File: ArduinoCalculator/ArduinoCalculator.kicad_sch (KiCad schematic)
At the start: 1 part, among them U1 NORA-W106-00B

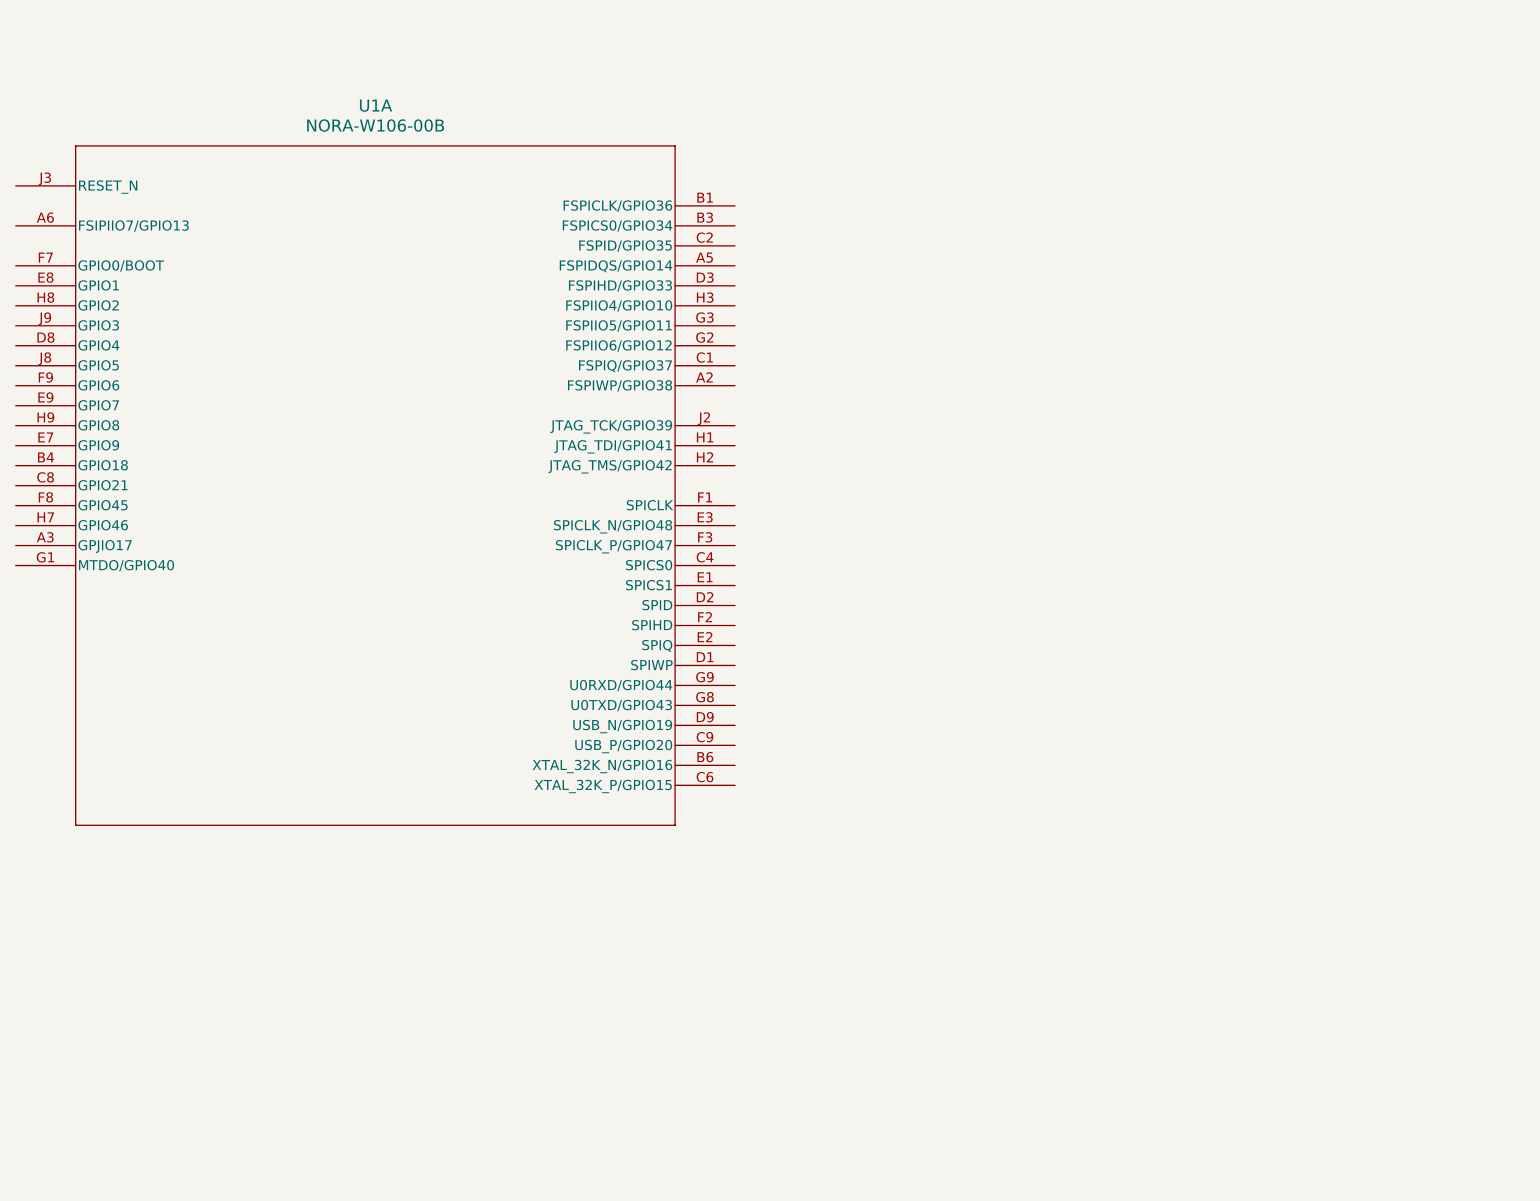
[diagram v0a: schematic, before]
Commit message: added NORA model
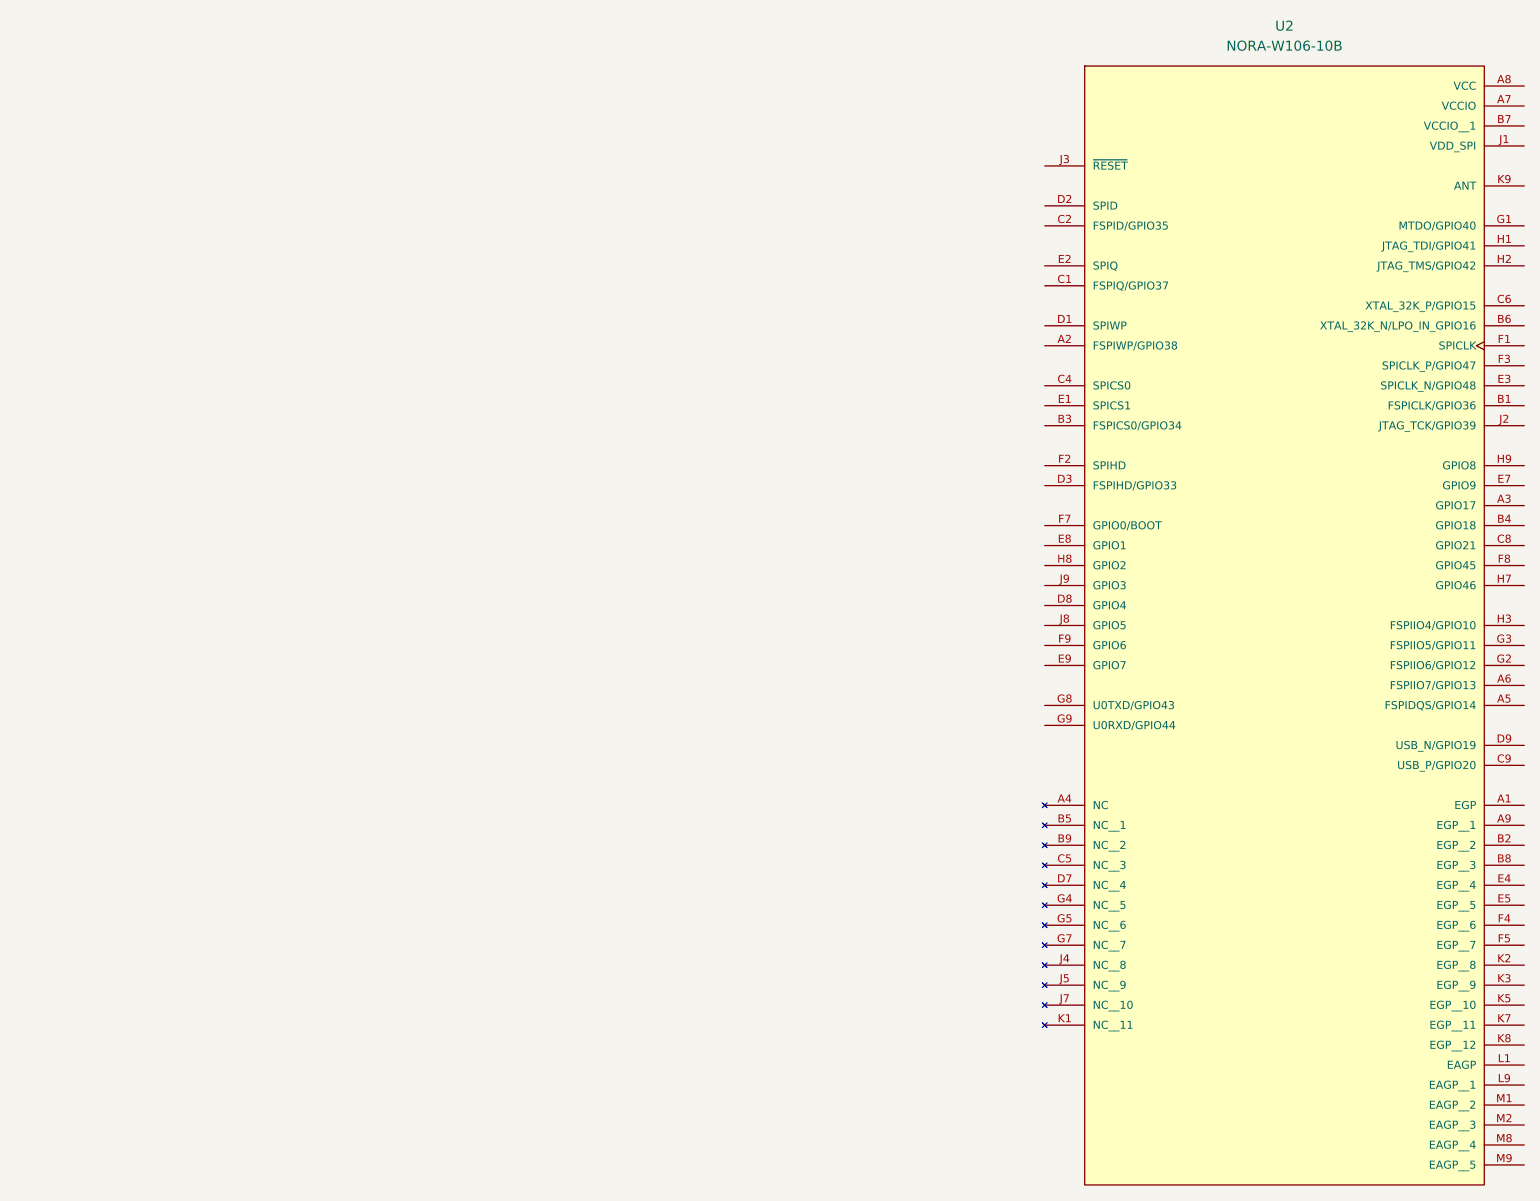
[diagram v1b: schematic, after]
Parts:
- removed U1: NORA-W106-00B, NORA-W10_UBL, symbol 2024-04-20_20-58-12:NORA-W106-00B
- added U2: NORA-W106-10B, footprints:NORA-W10_UBL, symbol NORA-W106-00B:NORA-W106-10B
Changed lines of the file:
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@@
 	(generator "eeschema")
 	(generator_version "8.0")
-	(paper "A4")
+	(paper "A3")
 	(title_block
 		(title "Arduino Calculator")
@@
 	)
 	(symbol
-		(lib_id "2024-04-20_20-58-12:NORA-W106-00B")
-		(at 72.39 60.96 0)
+		(lib_id "NORA-W106-00B:NORA-W106-10B")
+		(at 233.68 93.98 0)
 		(unit 1)
 		(exclude_from_sim no)
@@
 		(dnp no)
 		(fields_autoplaced yes)
-		(property "Reference" "U1"
-			(at 118.11 50.8 0)
-			(effects
-				(font
-					(size 1.524 1.524)
-				)
-			)
-		)
-		(property "Value" "NORA-W106-00B"
-			(at 118.11 53.34 0)
-			(effects
-				(font
-					(size 1.524 1.524)
-				)
-			)
-		)
-		(property "Footprint" "NORA-W10_UBL"
-			(at 72.39 60.96 0)
-			(effects
-				(font
-					(size 1.27 1.27)
-					(italic yes)
-				)
-				(hide yes)
-			)
-		)
-		(property "Datasheet" "NORA-W106-00B"
-			(at 72.39 60.96 0)
-			(effects
-				(font
-					(size 1.27 1.27)
-					(italic yes)
+		(property "Reference" "U2"
+			(at 233.68 40.64 0)
+			(effects
+				(font
+					(size 1.27 1.27)
+				)
+			)
+		)
+		(property "Value" "NORA-W106-10B"
+			(at 233.68 43.18 0)
+			(effects
+				(font
+					(size 1.27 1.27)
+				)
+			)
+		)
+		(property "Footprint" "footprints:NORA-W10_UBL"
+			(at 233.68 93.98 0)
+			(effects
+				(font
+					(size 1.27 1.27)
+				)
+				(justify bottom)
+				(hide yes)
+			)
+		)
+		(property "Datasheet" ""
+			(at 233.68 93.98 0)
+			(effects
+				(font
+					(size 1.27 1.27)
 				)
 				(hide yes)
@@
 		)
 		(property "Description" ""
-			(at 72.39 60.96 0)
-			(effects
-				(font
-					(size 1.27 1.27)
-				)
-				(hide yes)
-			)
+			(at 233.68 93.98 0)
+			(effects
+				(font
+					(size 1.27 1.27)
+				)
+				(hide yes)
+			)
+		)
+		(property "PARTREV" "R03"
+			(at 233.68 93.98 0)
+			(effects
+				(font
+					(size 1.27 1.27)
+				)
+				(justify bottom)
+				(hide yes)
+			)
+		)
+		(property "STANDARD" "Manufacturer recommendations"
+			(at 233.68 93.98 0)
+			(effects
+				(font
+					(size 1.27 1.27)
+				)
+				(justify bottom)
+				(hide yes)
+			)
+		)
+		(property "MAXIMUM_PACKAGE_HEIGHT" "1.9 mm"
+			(at 233.68 93.98 0)
+			(effects
+				(font
+					(size 1.27 1.27)
+				)
+				(justify bottom)
+				(hide yes)
+			)
+		)
+		(property "MANUFACTURER" "U-BLOX"
+			(at 233.68 93.98 0)
+			(effects
+				(font
+					(size 1.27 1.27)
+				)
+				(justify bottom)
+				(hide yes)
+			)
+		)
+		(pin "H1"
+		)
+		(pin "H2"
+		)
+		(pin "B4"
+		)
+		(pin "E7"
+		)
+		(pin "C5"
+		)
+		(pin "E9"
+		)
+		(pin "F2"
+		)
+		(pin "H3"
+		)
+		(pin "H7"
+		)
+		(pin "G5"
+		)
+		(pin "A5"
+		)
+		(pin "E3"
+		)
+		(pin "B7"
+		)
+		(pin "G3"
+		)
+		(pin "G8"
+		)
+		(pin "A6"
+		)
+		(pin "A7"
+		)
+		(pin "D9"
+		)
+		(pin "E2"
+		)
+		(pin "H8"
 		)
 		(pin "A8"
 		)
+		(pin "H9"
+		)
+		(pin "E4"
+		)
+		(pin "J1"
+		)
+		(pin "F9"
+		)
+		(pin "G9"
+		)
+		(pin "J2"
+		)
+		(pin "J3"
+		)
+		(pin "F5"
+		)
+		(pin "B3"
+		)
+		(pin "C9"
+		)
+		(pin "B2"
+		)
+		(pin "D7"
+		)
+		(pin "E1"
+		)
 		(pin "A9"
 		)
-		(pin "B7"
-		)
-		(pin "D7"
-		)
-		(pin "E4"
+		(pin "C1"
+		)
+		(pin "F1"
+		)
+		(pin "C8"
+		)
+		(pin "F3"
+		)
+		(pin "A1"
+		)
+		(pin "D1"
+		)
+		(pin "C6"
+		)
+		(pin "D8"
 		)
 		(pin "E5"
 		)
+		(pin "B5"
+		)
+		(pin "B9"
+		)
+		(pin "E8"
+		)
 		(pin "F4"
 		)
-		(pin "B4"
-		)
-		(pin "F5"
+		(pin "B8"
+		)
+		(pin "A4"
+		)
+		(pin "C2"
+		)
+		(pin "D3"
+		)
+		(pin "A3"
+		)
+		(pin "F7"
+		)
+		(pin "B6"
+		)
+		(pin "B1"
+		)
+		(pin "D2"
+		)
+		(pin "F8"
+		)
+		(pin "A2"
+		)
+		(pin "C4"
+		)
+		(pin "G1"
+		)
+		(pin "G2"
 		)
 		(pin "G4"
 		)
-		(pin "A6"
-		)
-		(pin "G3"
-		)
-		(pin "C4"
-		)
-		(pin "F9"
-		)
-		(pin "H2"
-		)
-		(pin "E8"
-		)
-		(pin "D8"
-		)
-		(pin "H9"
-		)
-		(pin "A2"
-		)
-		(pin "E1"
-		)
-		(pin "F1"
-		)
-		(pin "F7"
-		)
-		(pin "A4"
-		)
-		(pin "H3"
-		)
-		(pin "B6"
-		)
-		(pin "C1"
-		)
-		(pin "D1"
-		)
-		(pin "J3"
-		)
-		(pin "C9"
+		(pin "G7"
+		)
+		(pin "J5"
+		)
+		(pin "K1"
+		)
+		(pin "K3"
+		)
+		(pin "M9"
+		)
+		(pin "K8"
+		)
+		(pin "J9"
+		)
+		(pin "K9"
+		)
+		(pin "K2"
+		)
+		(pin "J4"
+		)
+		(pin "L1"
 		)
 		(pin "J8"
 		)
-		(pin "B3"
-		)
-		(pin "F3"
-		)
-		(pin "H1"
-		)
-		(pin "J9"
-		)
-		(pin "B2"
-		)
-		(pin "F2"
-		)
-		(pin "E7"
-		)
-		(pin "B5"
-		)
-		(pin "C2"
-		)
-		(pin "E3"
-		)
-		(pin "B1"
-		)
-		(pin "G1"
-		)
-		(pin "G8"
-		)
-		(pin "J2"
-		)
-		(pin "A1"
-		)
-		(pin "A3"
-		)
-		(pin "D2"
-		)
-		(pin "G2"
-		)
-		(pin "A7"
-		)
-		(pin "E2"
-		)
-		(pin "B8"
-		)
-		(pin "B9"
-		)
-		(pin "E9"
-		)
-		(pin "C5"
-		)
-		(pin "C6"
-		)
-		(pin "A5"
-		)
-		(pin "C8"
-		)
-		(pin "D3"
-		)
-		(pin "D9"
-		)
-		(pin "F8"
-		)
-		(pin "H7"
-		)
-		(pin "H8"
-		)
-		(pin "G9"
-		)
-		(pin "M9"
-		)
-		(pin "K8"
-		)
-		(pin "J5"
-		)
-		(pin "G7"
+		(pin "M1"
+		)
+		(pin "M8"
 		)
 		(pin "M2"
@@
 		(pin "J7"
 		)
-		(pin "L1"
-		)
-		(pin "J1"
-		)
-		(pin "J4"
-		)
-		(pin "K1"
+		(pin "K5"
+		)
+		(pin "L9"
 		)
 		(pin "K7"
-		)
-		(pin "K5"
-		)
-		(pin "K2"
-		)
-		(pin "K3"
-		)
-		(pin "K9"
-		)
-		(pin "G5"
-		)
-		(pin "L9"
-		)
-		(pin "M1"
-		)
-		(pin "M8"
 		)
 		(instances
 			(project "ArduinoCalculator"
 				(path "/bb8af01d-b51c-41f0-a39f-f8b4766b0d14"
-					(reference "U1")
+					(reference "U2")
 					(unit 1)
 				)

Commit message: adding some schematic work
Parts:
- added DS1: WC1602A, Display:WC1602A, symbol Display_Character:WC1602A
- added J1: Conn_01x04_Socket, Connector_PinHeader_2.54mm:PinHeader_1x04_P2.54mm_Vertical, symbol Connector:Conn_01x04_Socket
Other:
- note added: "Cheapest and simplest option is to go for a display with a I2C interface module. Then we can choose later how big lcd display is needed"
- note added: "This display is for show only - update footprint and 3d model"
- moved on the sheet: U2

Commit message: adde libs
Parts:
- added J10, J2, J3, J4, J5, J6, J7, J8, J9: Conn_01x01_Pin, symbol Connector:Conn_01x01_Pin
- added SW1: Push_Button, PCM_Switch_Keyboard_Cherry_MX:SW_Cherry_MX_PCB, symbol SL_Devices:Push_Button
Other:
- note added: "Capacitive touch pads"
- note added: "LCD display i2c header"
- moved on the sheet: J1

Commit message: slakd
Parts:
- removed J10, J2, J3, J4, J5, J6, J7, J8, J9: Conn_01x01_Pin, symbol Connector:Conn_01x01_Pin
- added J2: USB_C_Receptacle_USB2.0_16P, Connector_USB:USB_C_Receptacle_GCT_USB4105-xx-A_16P_TopMnt_Horizontal, symbol Connector:USB_C_Receptacle_USB2.0_16P
- added J3: PINHD_2x5_Male, Connector_PinHeader_2.54mm:PinHeader_2x05_P2.54mm_Vertical, symbol SL_Pin_Headers:PINHD_2x5_Male
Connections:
- new net: J2.A1 (GND), J2.A12 (GND), J2.B1 (GND), J2.B12 (GND)
- new net: J2.A4 (VBUS), J2.A9 (VBUS), J2.B4 (VBUS), J2.B9 (VBUS)
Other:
- note added: "Arduino Nano esp32 schematics: https://docs.arduino.cc/resources/schematics/ABX00083-schematics.pdf"
- note added: "Battery charging"
- note added: "Break out Headers for cool stuff later"
- note added: "Interesting video on battery and charging https://www.youtube.com/watch?v=cDRjSY4ImSo"
- note added: "Voltage rtegulator. Either 5v usb to 3.3v or from lipo to 3.3v"
- note added: "https://docs.espressif.com/projects/esp-idf/en/latest/esp32s3/api-reference/peripherals/usb_device.html"
- moved on the sheet: SW1
